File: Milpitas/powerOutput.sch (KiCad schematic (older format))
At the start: 26 parts

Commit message: Updated some silly mistakes
Updated some silly mistakes,
- capacitor decoupled to gnd
- Added option for jumper control to 2 24V modules
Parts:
- F? (x13): symbol Device:Fuse -> Milpitas-rescue:Fuse-Device
- J? (x10): symbol Connector:Conn_01x02_Female -> Milpitas-rescue:Conn_01x02_Female-Connector
- J?: value SPARE -> SPARE_12V; symbol Connector:Conn_01x02_Female -> Milpitas-rescue:Conn_01x02_Female-Connector
- J? (x2): value SPARE -> SPARE_5V; symbol Connector:Conn_01x02_Female -> Milpitas-rescue:Conn_01x02_Female-Connector
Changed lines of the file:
@@
 EESchema Schematic File Version 4
 LIBS:Milpitas-cache
-EELAYER 26 0
+EELAYER 29 0
 EELAYER END
 $Descr A4 11693 8268
@@
 5V_OUTPUT
 $Comp
-L Connector:Conn_01x02_Female J?
+L Milpitas-rescue:Conn_01x02_Female-Connector J?
 U 1 1 5DE45734
 P 9100 1000
@@
 $EndComp
 $Comp
-L Connector:Conn_01x02_Female J?
+L Milpitas-rescue:Conn_01x02_Female-Connector J?
 U 1 1 5DE45799
 P 9100 1350
@@
 $EndComp
 $Comp
-L Connector:Conn_01x02_Female J?
+L Milpitas-rescue:Conn_01x02_Female-Connector J?
 U 1 1 5DE457E2
 P 9100 1700
@@
 $EndComp
 $Comp
-L Connector:Conn_01x02_Female J?
+L Milpitas-rescue:Conn_01x02_Female-Connector J?
 U 1 1 5DE45815
 P 9100 2050
@@
 24V OUTPUTS
 $Comp
-L Connector:Conn_01x02_Female J?
+L Milpitas-rescue:Conn_01x02_Female-Connector J?
 U 1 1 5DE45CB1
 P 9050 3000
@@
 $EndComp
 $Comp
-L Connector:Conn_01x02_Female J?
+L Milpitas-rescue:Conn_01x02_Female-Connector J?
 U 1 1 5DE45D08
 P 9050 3400
@@
 $EndComp
 $Comp
-L Connector:Conn_01x02_Female J?
+L Milpitas-rescue:Conn_01x02_Female-Connector J?
 U 1 1 5DE4632E
 P 9050 3800
@@
 $EndComp
 $Comp
-L Connector:Conn_01x02_Female J?
+L Milpitas-rescue:Conn_01x02_Female-Connector J?
 U 1 1 5DE4637B
 P 9050 4200
@@
 $EndComp
 $Comp
-L Connector:Conn_01x02_Female J?
+L Milpitas-rescue:Conn_01x02_Female-Connector J?
 U 1 1 5DE4657D
 P 9100 2400
@@
 $EndComp
 $Comp
-L Connector:Conn_01x02_Female J?
+L Milpitas-rescue:Conn_01x02_Female-Connector J?
 U 1 1 5DE467B2
 P 9050 4650
 F 0 "J?" H 9077 4626 50  0000 L CNN
-F 1 "SPARE" H 9077 4535 50  0000 L CNN
+F 1 "SPARE_12V" H 9077 4535 50  0000 L CNN
 F 2 "" H 9050 4650 50  0001 C CNN
 F 3 "~" H 9050 4650 50  0001 C CNN
@@
 12V OUTPUTS
 $Comp
-L Connector:Conn_01x02_Female J?
+L Milpitas-rescue:Conn_01x02_Female-Connector J?
 U 1 1 5DE46BA5
 P 9050 5400
@@
 $EndComp
 $Comp
-L Connector:Conn_01x02_Female J?
+L Milpitas-rescue:Conn_01x02_Female-Connector J?
 U 1 1 5DE46C14
 P 9050 5750
 F 0 "J?" H 9077 5726 50  0000 L CNN
-F 1 "SPARE" H 9077 5635 50  0000 L CNN
+F 1 "SPARE_5V" H 9077 5635 50  0000 L CNN
 F 2 "" H 9050 5750 50  0001 C CNN
 F 3 "~" H 9050 5750 50  0001 C CNN
@@
 $EndComp
 $Comp
-L Connector:Conn_01x02_Female J?
+L Milpitas-rescue:Conn_01x02_Female-Connector J?
 U 1 1 5DE46C84
 P 9050 6100
 F 0 "J?" H 9077 6076 50  0000 L CNN
-F 1 "SPARE" H 9077 5985 50  0000 L CNN
+F 1 "SPARE_5V" H 9077 5985 50  0000 L CNN
 F 2 "" H 9050 6100 50  0001 C CNN
 F 3 "~" H 9050 6100 50  0001 C CNN
@@
 5V OUTPUTS
 $Comp
-L power:GND #PWR?
+L Milpitas-rescue:GND-power #PWR?
 U 1 1 5DE4BE12
 P 8800 1100
@@
 	8800 1100 8900 1100
 $Comp
-L power:GND #PWR?
+L Milpitas-rescue:GND-power #PWR?
 U 1 1 5DE4C39E
 P 8800 1450
@@
 	8800 1450 8900 1450
 $Comp
-L power:GND #PWR?
+L Milpitas-rescue:GND-power #PWR?
 U 1 1 5DE4C58E
 P 8800 1800
@@
 	8800 1800 8900 1800
 $Comp
-L power:GND #PWR?
+L Milpitas-rescue:GND-power #PWR?
 U 1 1 5DE4C80E
 P 8800 2150
@@
 	8800 2150 8900 2150
 $Comp
-L power:GND #PWR?
+L Milpitas-rescue:GND-power #PWR?
 U 1 1 5DE4CCB1
 P 8800 2500
@@
 	8800 2500 8900 2500
 $Comp
-L Device:Fuse F?
+L Milpitas-rescue:Fuse-Device F?
 U 1 1 5DE4DFEB
 P 8550 1000
@@
 $EndComp
 $Comp
-L Device:Fuse F?
+L Milpitas-rescue:Fuse-Device F?
 U 1 1 5DE4E09E
 P 8550 1350
@@
 $EndComp
 $Comp
-L Device:Fuse F?
+L Milpitas-rescue:Fuse-Device F?
 U 1 1 5DE4E0DA
 P 8550 1700
@@
 $EndComp
 $Comp
-L Device:Fuse F?
+L Milpitas-rescue:Fuse-Device F?
 U 1 1 5DE4E114
 P 8550 2050
@@
 $EndComp
 $Comp
-L Device:Fuse F?
+L Milpitas-rescue:Fuse-Device F?
 U 1 1 5DE4E150
 P 8550 2400
@@
 	8700 2400 8900 2400
 $Comp
-L power:GND #PWR?
+L Milpitas-rescue:GND-power #PWR?
 U 1 1 5DE4F477
 P 8750 3500
@@
 	8750 3500 8850 3500
 $Comp
-L Device:Fuse F?
+L Milpitas-rescue:Fuse-Device F?
 U 1 1 5DE4F47E
 P 8500 3400
@@
 	8650 3400 8850 3400
 $Comp
-L power:GND #PWR?
+L Milpitas-rescue:GND-power #PWR?
 U 1 1 5DE4F800
 P 8750 3100
@@
 	8750 3100 8850 3100
 $Comp
-L Device:Fuse F?
+L Milpitas-rescue:Fuse-Device F?
 U 1 1 5DE4F807
 P 8500 3000
@@
 	8650 3000 8850 3000
 $Comp
-L power:GND #PWR?
+L Milpitas-rescue:GND-power #PWR?
 U 1 1 5DE4FF36
 P 8750 3900
@@
 	8750 3900 8850 3900
 $Comp
-L Device:Fuse F?
+L Milpitas-rescue:Fuse-Device F?
 U 1 1 5DE4FF3D
 P 8500 3800
@@
 	8650 3800 8850 3800
 $Comp
-L power:GND #PWR?
+L Milpitas-rescue:GND-power #PWR?
 U 1 1 5DE509B3
 P 8750 4300
@@
 	8750 4300 8850 4300
 $Comp
-L Device:Fuse F?
+L Milpitas-rescue:Fuse-Device F?
 U 1 1 5DE509BA
 P 8500 4200
@@
 	8650 4200 8850 4200
 $Comp
-L power:GND #PWR?
+L Milpitas-rescue:GND-power #PWR?
 U 1 1 5DE5147C
 P 8750 4750
@@
 	8750 4750 8850 4750
 $Comp
-L Device:Fuse F?
+L Milpitas-rescue:Fuse-Device F?
 U 1 1 5DE51483
 P 8500 4650
@@
 	8650 4650 8850 4650
 $Comp
-L power:GND #PWR?
+L Milpitas-rescue:GND-power #PWR?
 U 1 1 5DE53CBD
 P 8750 5500
@@
 	8750 5500 8850 5500
 $Comp
-L Device:Fuse F?
+L Milpitas-rescue:Fuse-Device F?
 U 1 1 5DE53CC4
 P 8500 5400
@@
 	8650 5400 8850 5400
 $Comp
-L power:GND #PWR?
+L Milpitas-rescue:GND-power #PWR?
 U 1 1 5DE546BD
 P 8750 5850
@@
 	8750 5850 8850 5850
 $Comp
-L Device:Fuse F?
+L Milpitas-rescue:Fuse-Device F?
 U 1 1 5DE546C4
 P 8500 5750
@@
 	8650 5750 8850 5750
 $Comp
-L power:GND #PWR?
+L Milpitas-rescue:GND-power #PWR?
 U 1 1 5DE54C2C
 P 8750 6200
@@
 	8750 6200 8850 6200
 $Comp
-L Device:Fuse F?
+L Milpitas-rescue:Fuse-Device F?
 U 1 1 5DE54C33
 P 8500 6100

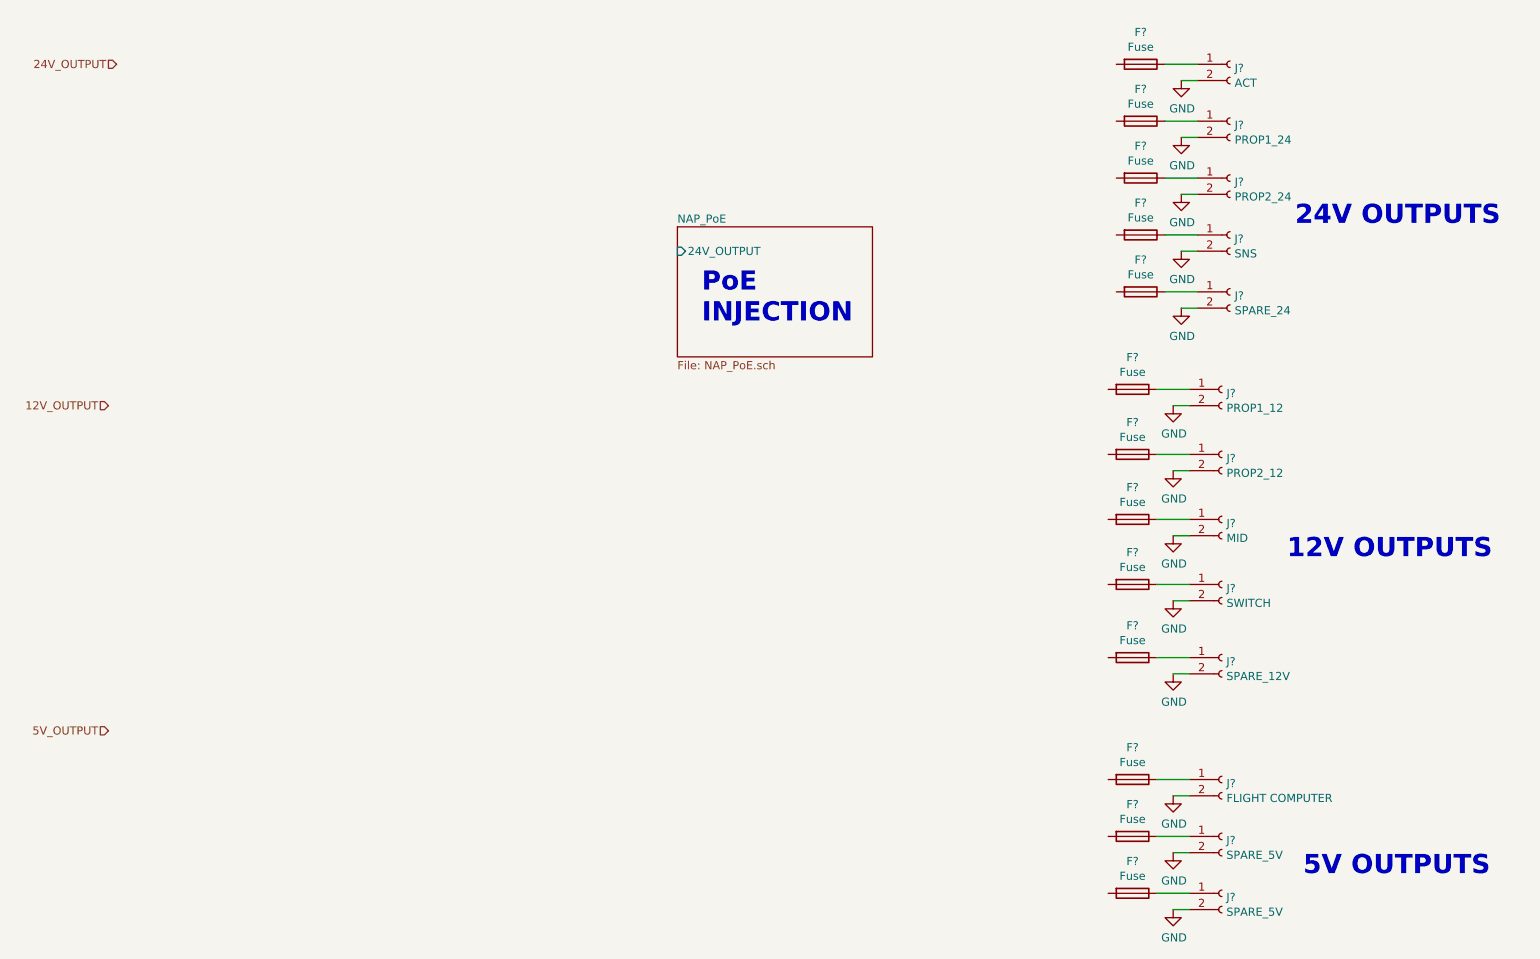
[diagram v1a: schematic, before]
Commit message: Updated input control circuitry. Rationale and calcs in google drive.
Updated and added all part numbers for input protection circuitry. Not yet ready for review.
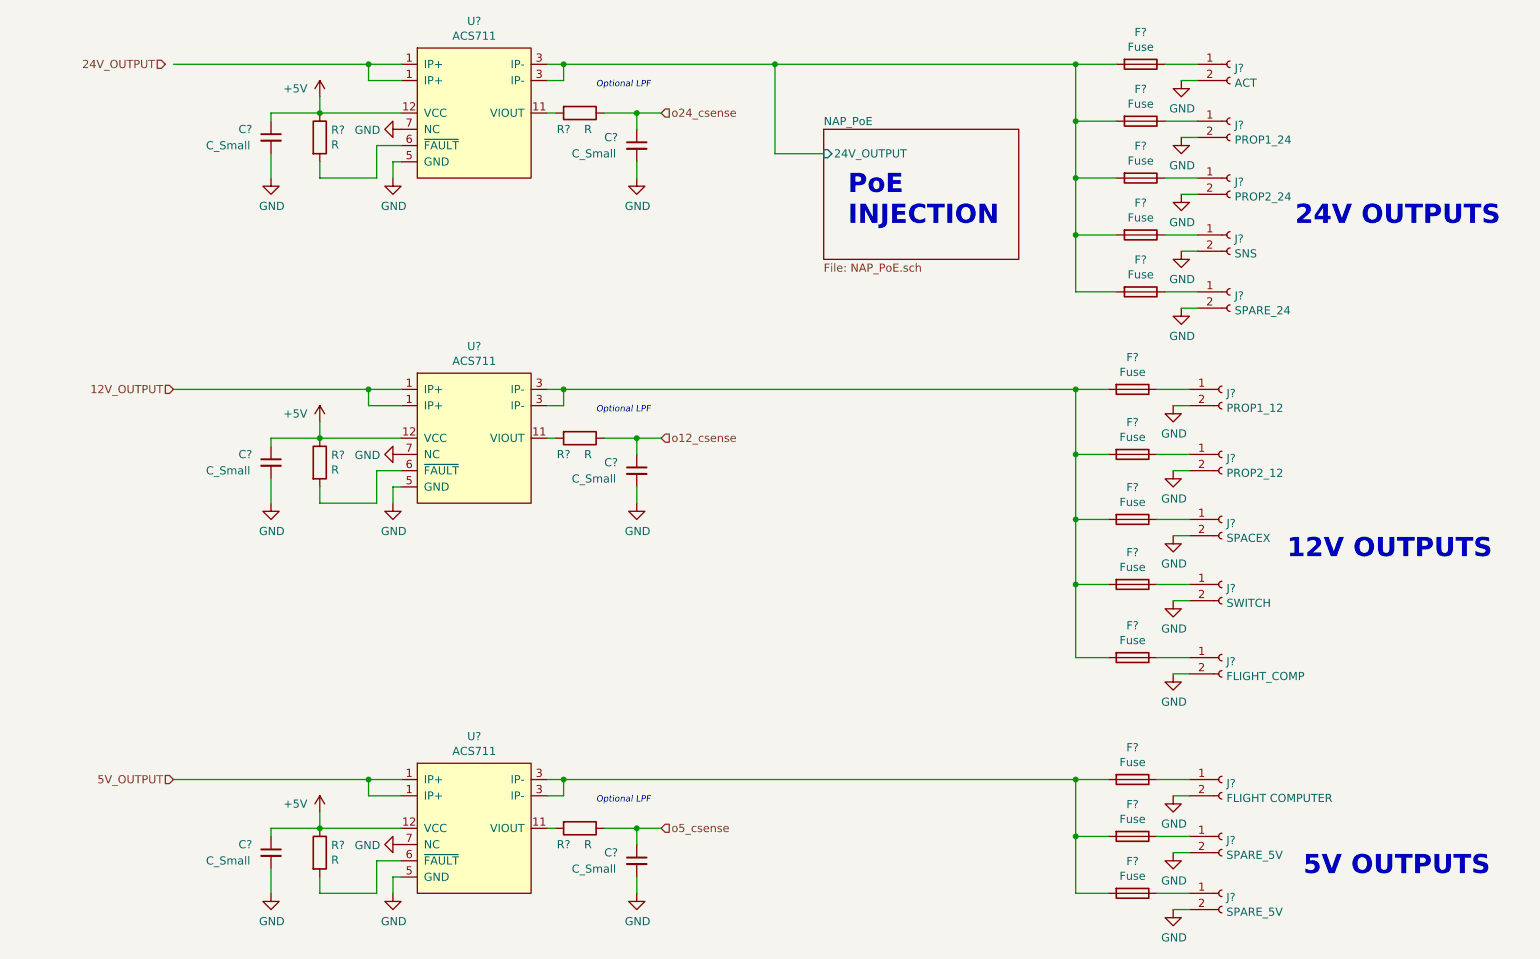
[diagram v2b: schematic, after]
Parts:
- added C? (x6): C_Small, symbol Device:C_Small
- added R? (x6): R, symbol Device:R
- added U? (x3): ACS711, symbol Milpitas-rescue:ACS711-hypersymbols
- J?: value MID -> SPACEX
- J?: value SPARE_12V -> FLIGHT_COMP
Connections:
- net 12V_OUTPUT: now also U?.1 (IP+)
- net 5V_OUTPUT: now also U?.1 (IP+)
- net GND: now also C?.2, C?.2, C?.2, C?.2, C?.2, C?.2, U?.5 (GND), U?.5 (GND), U?.5 (GND), U?.7 (NC), U?.7 (NC), U?.7 (NC)
- net NAP_PoE/24V_OUTPUT: now also F?.2, F?.2, F?.2, F?.2, F?.2, U?.3 (IP-)
- net at F?.2: now also F?.2, F?.2, F?.2, F?.2, U?.3 (IP-)
- net at F?.2: now also F?.2, F?.2, U?.3 (IP-)
- new net: R?.2, U?.6 (~FAULT) (x3)
- new net: R?.2, U?.11 (VIOUT) (x3)
- new net +5V: C?.1, C?.1, C?.1, R?.1, R?.1, R?.1, U?.12 (VCC), U?.12 (VCC), U?.12 (VCC)
- new net o12_csense: C?.1, R?.1
- new net o24_csense: C?.1, R?.1
- new net o5_csense: C?.1, R?.1
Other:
- note added: "Optional LPF"
